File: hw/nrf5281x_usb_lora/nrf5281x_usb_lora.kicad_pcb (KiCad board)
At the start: 2 copper layers, 49.5 x 19 mm, 36 parts, among them J1 USB_A, J3 TC2030-CTX, SW1 RST, U1 MIC550X, U2 FT234XD, U3 NRF52811-QFAA, U4 E22-X00M22S, Y1 32.768kHz

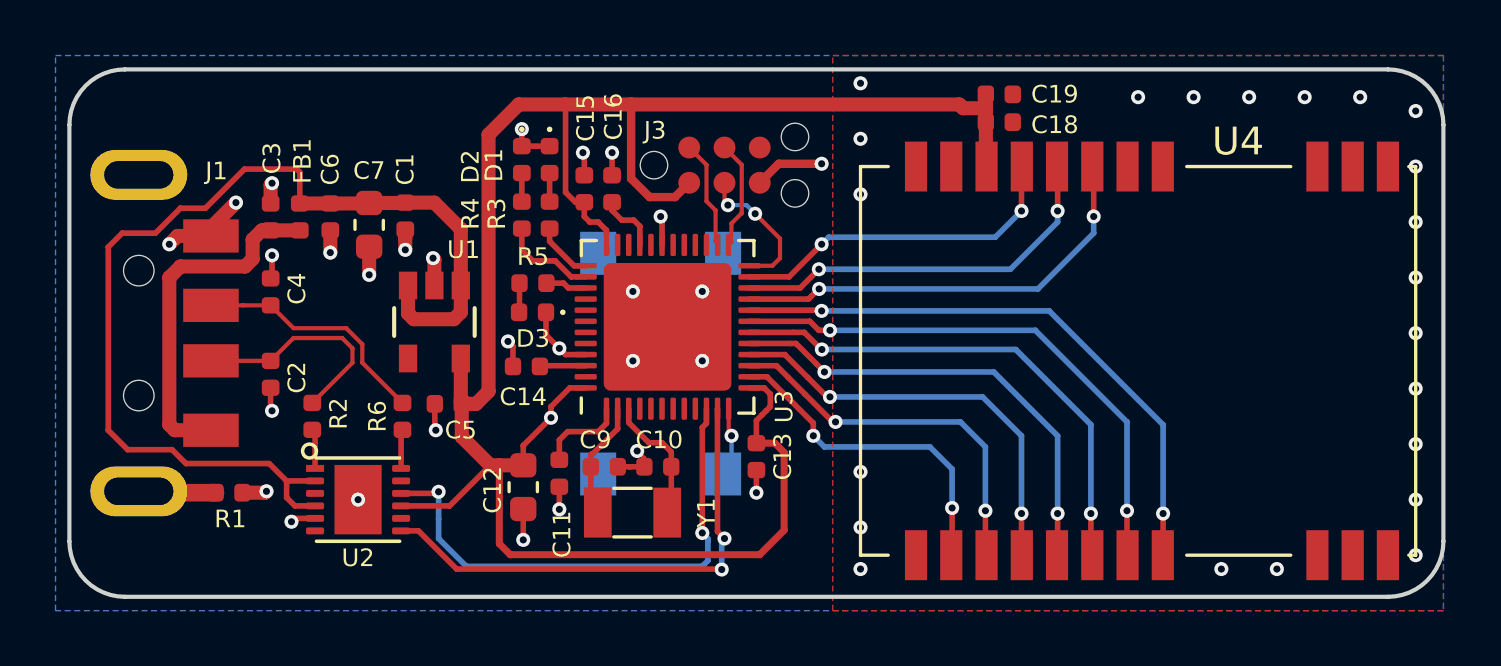
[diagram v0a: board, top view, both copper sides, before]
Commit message: Updated nrf5281x_usb_lora to be smaller
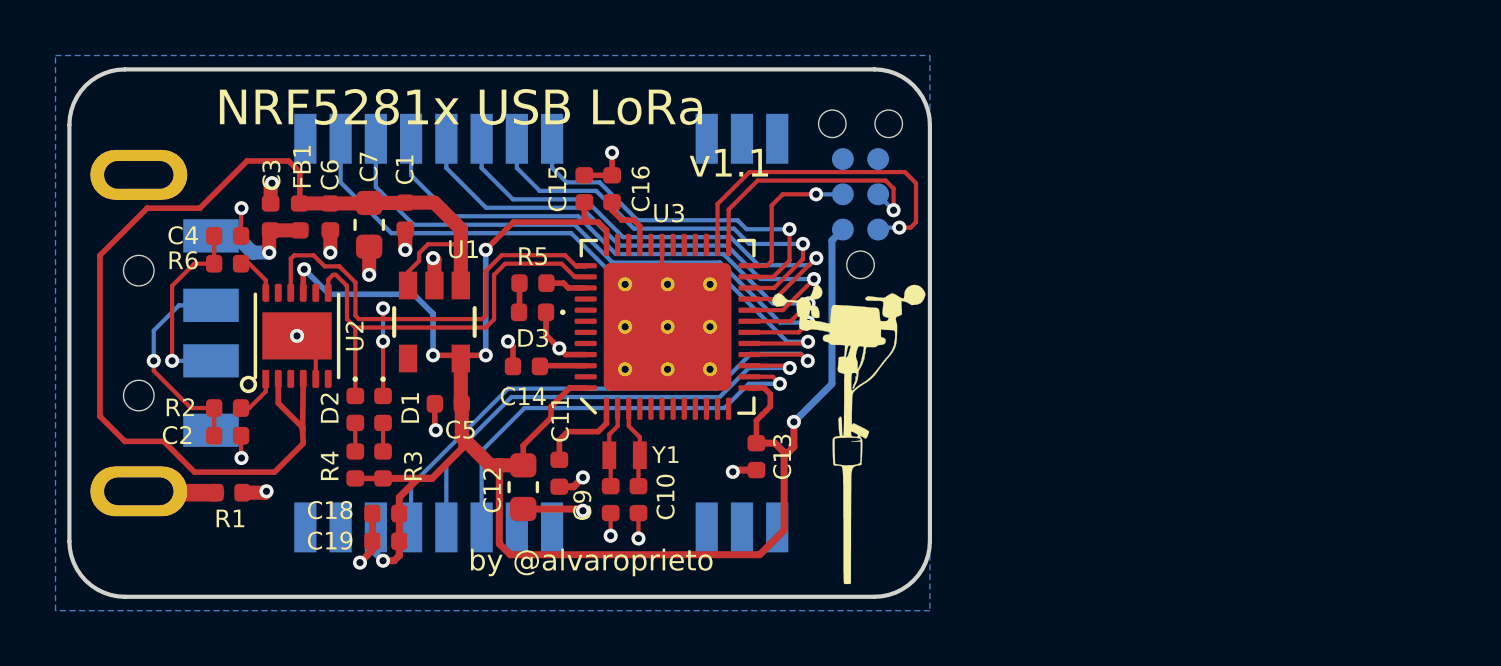
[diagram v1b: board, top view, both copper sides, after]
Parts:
- removed REF**: OSHW-Logo_7.5x8mm_SilkScreen, Symbol:OSHW-Logo_7.5x8mm_SilkScreen
- removed SW1: RST, alvarop:PTS645SM43SMTR92
- added G***: LOGO, alvarop:weather_station_tiny, F.Cu at (195.6, 93.6)
- J1, J3, U4: moved to B.Cu
- U3: footprint Package_DFN_QFN:QFN-48-1EP_6x6mm_P0.4mm_EP4.6x4.6mm -> alvarop:NRF52811-QFN48-VIAS
- Y1: footprint Crystal:Crystal_SMD_3215-2Pin_3.2x1.5mm -> alvarop:ABS05
- moved C19 27.3 mm to (178.9, 97.5), turned to 180 degrees
- moved C18 26.2 mm to (178.9, 96.5), turned to 180 degrees
- moved U4 25.6 mm to (193.0, 97.0)
- moved D1 10.8 mm to (178.8, 92.8)
- moved D2 10.8 mm to (177.8, 92.8)
- moved R3 10.8 mm to (178.8, 94.8)
- moved R4 10.8 mm to (177.8, 94.8)
- moved R6 8.36 mm to (173.2, 87.5), turned to 0 degrees
- moved U2 6.30 mm to (175.7, 90.1), turned to 90 degrees
- moved J3 5.01 mm to (196.0, 85.0), turned to 90 degrees
- moved R2 3.06 mm to (173.2, 92.7), turned to 180 degrees
- moved C2 2.70 mm to (173.2, 93.7), turned to 0 degrees
- moved C4 2.54 mm to (173.2, 86.5), turned to 0 degrees
- moved Y1 2.09 mm to (187.5, 94.4), turned to 0 degrees
- moved C10 1.37 mm to (188.0, 96.0), turned to 270 degrees
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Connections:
- D1 pad 1: GND -> /UART_TX
- D2 pad 1: GND -> /UART_RX
- R3 pad 2: /TX_LED -> +3V3
- R4 pad 2: /RX_LED -> +3V3
- U3 pad 10: /UART_TX -> Net-(U3-Pad10)
- U3 pad 11: /UART_RX -> Net-(U3-Pad11)
- U3 pad 12: /BOOT -> Net-(U3-Pad12)
- U3 pad 14: /E22_DIO1 -> /E22_RXEN
- U3 pad 15: /E22_BUSY -> /E22_TXEN
- U3 pad 16: /E22_NRST -> /E22_DIO2
- U3 pad 17: /MISO -> /E22_DIO1
- U3 pad 18: /MOSI -> /E22_BUSY
- U3 pad 19: /SCK -> /E22_NRST
- U3 pad 20: /E22_NSS -> /MISO
- U3 pad 21: /E22_RXEN -> /MOSI
- U3 pad 22: /E22_TXEN -> /SCK
- U3 pad 23: /E22_DIO2 -> /E22_NSS
- U3 pad 37: /TX_LED -> /UART_TX
- U3 pad 38: /RX_LED -> /UART_RX
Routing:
- net /E22_DIO1: track 12.1 -> 22.9 mm, vias 2 -> 1
- net Net-(C3-Pad2): track 12.7 -> 4.22 mm, vias 0 -> 1
- net /SWDIO: track 3.93 -> 12.1 mm, vias 0 -> 1
- net /E22_NSS: track 21.4 -> 13.3 mm, vias 2 -> 1
- net /E22_BUSY: track 13.6 -> 21.6 mm, vias 2 -> 1
- net /E22_DIO2: track 12.4 -> 20.1 mm, vias 2 -> 1
- net +3V3: track 76.4 -> 68.9 mm, vias 1 -> 6
- net /SWCLK: track 3.96 -> 9.35 mm, vias 0 -> 1
- net /E22_NRST: track 15.3 -> 19.9 mm, vias 2 -> 1
- net /SCK: track 19.9 -> 15.4 mm, vias 2 -> 1
- net /E22_TXEN: track 14.1 -> 17.6 mm, vias 2 -> 1
- net /RX_LED: track 3.47 -> 0.00 mm
- net /BOOT: track 2.52 -> 0.00 mm, vias 1 -> 0
- net GND: track 26.7 -> 24.4 mm, vias 50 -> 19
- net /UART_RX: track 18.1 -> 15.9 mm, vias 2 -> 0
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- removed copper zone on F.Cu, net GND
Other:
- board size 49.5 x 19 mm -> 31 x 19 mm
- board text added: "NRF5281x USB LoRa"
- board text added: "by @alvaroprieto"
- board text added: "v1.1"
- board text removed: "BOOT"
- board text removed: "NRF52811_USB_LoRa v1.0 by @alvaroprieto"
